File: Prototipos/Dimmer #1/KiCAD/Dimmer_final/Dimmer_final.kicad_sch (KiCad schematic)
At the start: 23 parts, among them J2 Conn_01x02, K1 SRD-05VDC-SL-C, Q1 BC548B, Q2 BT137, U1 MOC3021M, U2 EL817

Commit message: Retoques finales placa dimmer
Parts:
- added TP1, TP2: TestPoint, TestPoint:TestPoint_Loop_D1.80mm_Drill1.0mm_Beaded, symbol Connector:TestPoint
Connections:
- net 48Vca_L: now also TP1.1
- net LOAD_L: now also TP2.1
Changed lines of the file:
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@@
+	)
+	(junction
+		(at 59.69 82.55)
+		(diameter 0)
+		(color 0 0 0 0)
+	)
+	(junction
+		(at 53.34 40.64)
+		(diameter 0)
+		(color 0 0 0 0)
 	)
 	(junction
@@
 	(wire
 		(pts
+			(xy 59.69 82.55) (xy 63.5 82.55)
+		)
+		(stroke
+			(width 0)
+			(type default)
+		)
+	)
+	(wire
+		(pts
 			(xy 96.52 115.57) (xy 99.06 115.57)
 		)
@@
 	(wire
 		(pts
-			(xy 46.99 40.64) (xy 63.5 40.64)
+			(xy 46.99 40.64) (xy 53.34 40.64)
 		)
 		(stroke
@@
 	(wire
 		(pts
+			(xy 53.34 40.64) (xy 63.5 40.64)
+		)
+		(stroke
+			(width 0)
+			(type default)
+		)
+	)
+	(wire
+		(pts
 			(xy 107.95 115.57) (xy 104.14 115.57)
 		)
@@
 	(wire
 		(pts
-			(xy 57.15 82.55) (xy 63.5 82.55)
+			(xy 57.15 82.55) (xy 59.69 82.55)
 		)
 		(stroke
@@
 	)
 	(symbol
+		(lib_id "Connector:TestPoint")
+		(at 59.69 82.55 0)
+		(unit 1)
+		(exclude_from_sim no)
+		(in_bom yes)
+		(on_board yes)
+		(dnp no)
+		(property "Reference" "TP2"
+			(at 57.912 77.47 0)
+			(effects
+				(font
+					(size 1.27 1.27)
+				)
+				(justify left)
+			)
+		)
+		(property "Value" "TestPoint"
+			(at 53.34 79.502 0)
+			(effects
+				(font
+					(size 1.27 1.27)
+				)
+				(justify left)
+				(hide yes)
+			)
+		)
+		(property "Footprint" "TestPoint:TestPoint_Loop_D1.80mm_Drill1.0mm_Beaded"
+			(at 64.77 82.55 0)
+			(effects
+				(font
+					(size 1.27 1.27)
+				)
+				(hide yes)
+			)
+		)
+		(property "Datasheet" "~"
+			(at 64.77 82.55 0)
+			(effects
+				(font
+					(size 1.27 1.27)
+				)
+				(hide yes)
+			)
+		)
+		(property "Description" "test point"
+			(at 59.69 82.55 0)
+			(effects
+				(font
+					(size 1.27 1.27)
+				)
+				(hide yes)
+			)
+		)
+		(pin "1"
+		)
+		(instances
+			(project ""
+				(path "/7934e872-2b7f-4f8f-a0b6-741d97320597"
+					(reference "TP2")
+					(unit 1)
+				)
+			)
+		)
+	)
+	(symbol
 		(lib_id "Proyecto_Final:PCIE_x4_NSH")
 		(at 210.82 62.23 0)
@@
 					(unit 1)
 				)
+			)
+		)
+	)
+	(symbol
+		(lib_id "Connector:TestPoint")
+		(at 53.34 40.64 0)
+		(unit 1)
+		(exclude_from_sim no)
+		(in_bom yes)
+		(on_board yes)
+		(dnp no)
+		(property "Reference" "TP1"
+			(at 51.562 35.56 0)
+			(effects
+				(font
+					(size 1.27 1.27)
+				)
+				(justify left)
+			)
+		)
+		(property "Value" "TestPoint"
+			(at 55.88 38.6079 0)
+			(effects
+				(font
+					(size 1.27 1.27)
+				)
+				(justify left)
+				(hide yes)
+			)
+		)
+		(property "Footprint" "TestPoint:TestPoint_Loop_D1.80mm_Drill1.0mm_Beaded"
+			(at 58.42 40.64 0)
+			(effects
+				(font
+					(size 1.27 1.27)
+				)
+				(hide yes)
+			)
+		)
+		(property "Datasheet" "~"
+			(at 58.42 40.64 0)
+			(effects
+				(font
+					(size 1.27 1.27)
+				)
+				(hide yes)
+			)
+		)
+		(property "Description" "test point"
+			(at 53.34 40.64 0)
+			(effects
+				(font
+					(size 1.27 1.27)
+				)
+				(hide yes)
+			)
+		)
+		(pin "1"
+		)
+		(instances
+			(project ""
+				(path "/7934e872-2b7f-4f8f-a0b6-741d97320597"
+					(reference "TP1")
+					(unit 1)
+				)

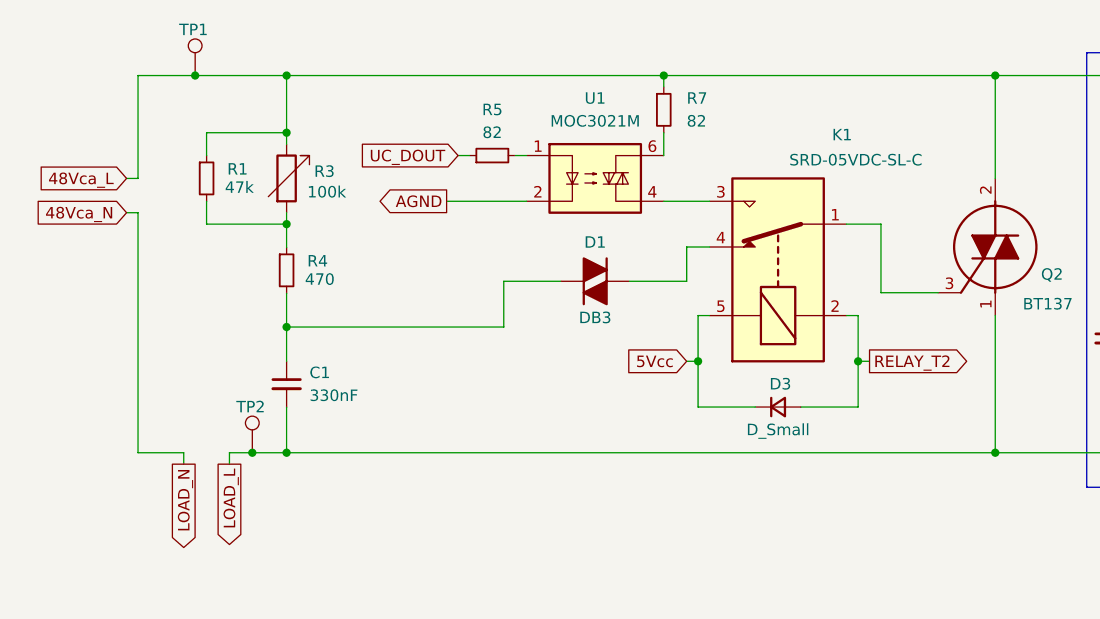
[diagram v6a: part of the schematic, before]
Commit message: Agregar TPs nuevos y correcciones varias
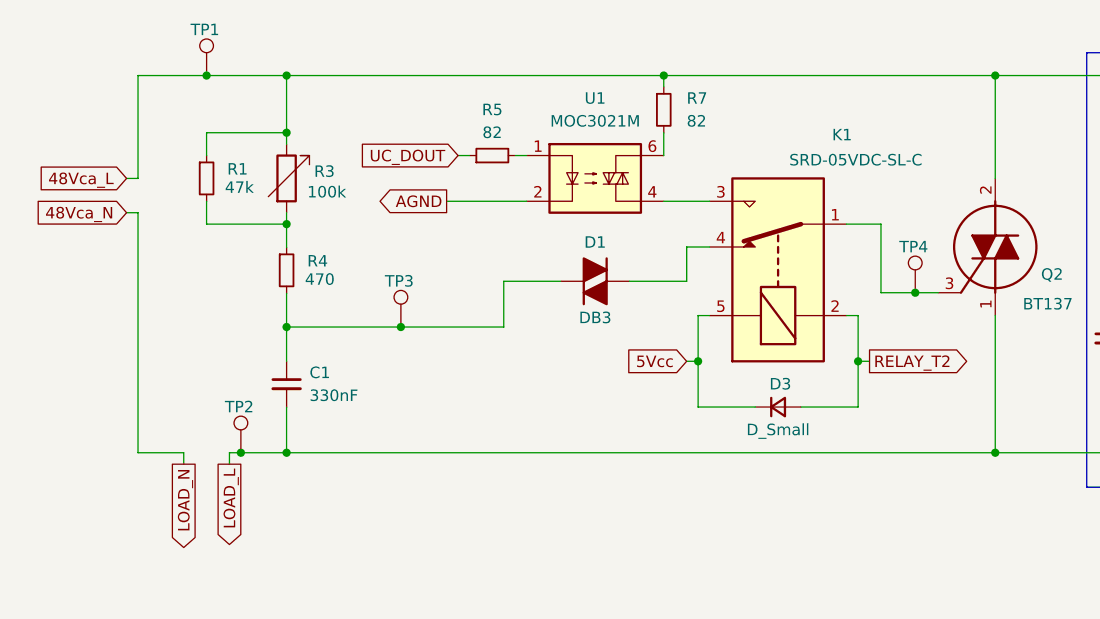
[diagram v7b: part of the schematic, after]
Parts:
- added TP3, TP4: TestPoint, TestPoint:TestPoint_Loop_D1.80mm_Drill1.0mm_Beaded, symbol Connector:TestPoint
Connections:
- net at C1.1, D1.1 (K), R4.2: now also TP3.1
- net at K1.1, Q2.3 (G): now also TP4.1
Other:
- moved on the sheet: TP1, TP2
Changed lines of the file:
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@@
 	)
 	(junction
-		(at 127 72.39)
+		(at 58.42 82.55)
 		(diameter 0)
 		(color 0 0 0 0)
 	)
 	(junction
-		(at 142.24 82.55)
+		(at 133.35 64.77)
 		(diameter 0)
 		(color 0 0 0 0)
 	)
 	(junction
-		(at 59.69 82.55)
+		(at 127 72.39)
 		(diameter 0)
 		(color 0 0 0 0)
 	)
 	(junction
-		(at 53.34 40.64)
+		(at 142.24 82.55)
 		(diameter 0)
 		(color 0 0 0 0)
@@
 	)
 	(junction
+		(at 76.2 68.58)
+		(diameter 0)
+		(color 0 0 0 0)
+	)
+	(junction
+		(at 54.61 40.64)
+		(diameter 0)
+		(color 0 0 0 0)
+	)
+	(junction
 		(at 63.5 68.58)
 		(diameter 0)
@@
 	(wire
 		(pts
-			(xy 105.41 54.61) (xy 110.49 54.61)
+			(xy 58.42 82.55) (xy 63.5 82.55)
 		)
 		(stroke
@@
 	(wire
 		(pts
-			(xy 154.94 72.39) (xy 154.94 82.55)
+			(xy 105.41 54.61) (xy 110.49 54.61)
 		)
 		(stroke
@@
 	(wire
 		(pts
-			(xy 120.65 77.47) (xy 127 77.47)
+			(xy 154.94 72.39) (xy 154.94 82.55)
 		)
 		(stroke
@@
 	(wire
 		(pts
-			(xy 59.69 82.55) (xy 63.5 82.55)
+			(xy 120.65 77.47) (xy 127 77.47)
 		)
 		(stroke
@@
 	(wire
 		(pts
-			(xy 46.99 40.64) (xy 53.34 40.64)
+			(xy 46.99 40.64) (xy 54.61 40.64)
+		)
+		(stroke
+			(width 0)
+			(type default)
+		)
+	)
+	(wire
+		(pts
+			(xy 133.35 64.77) (xy 135.89 64.77)
 		)
 		(stroke
@@
 	(wire
 		(pts
-			(xy 129.54 64.77) (xy 135.89 64.77)
+			(xy 129.54 64.77) (xy 133.35 64.77)
 		)
 		(stroke
@@
 	(wire
 		(pts
+			(xy 76.2 68.58) (xy 87.63 68.58)
+		)
+		(stroke
+			(width 0)
+			(type default)
+		)
+	)
+	(wire
+		(pts
 			(xy 129.54 124.46) (xy 132.08 124.46)
 		)
@@
 	(wire
 		(pts
-			(xy 63.5 68.58) (xy 87.63 68.58)
+			(xy 63.5 68.58) (xy 76.2 68.58)
 		)
 		(stroke
@@
 	(wire
 		(pts
-			(xy 53.34 40.64) (xy 63.5 40.64)
-		)
-		(stroke
-			(width 0)
-			(type default)
-		)
-	)
-	(wire
-		(pts
 			(xy 107.95 115.57) (xy 104.14 115.57)
 		)
@@
 	(wire
 		(pts
-			(xy 57.15 82.55) (xy 59.69 82.55)
+			(xy 57.15 82.55) (xy 58.42 82.55)
 		)
 		(stroke
@@
 	(wire
 		(pts
+			(xy 54.61 40.64) (xy 63.5 40.64)
+		)
+		(stroke
+			(width 0)
+			(type default)
+		)
+	)
+	(wire
+		(pts
 			(xy 87.63 63.5) (xy 93.98 63.5)
 		)
@@
 	(symbol
 		(lib_id "Connector:TestPoint")
-		(at 59.69 82.55 0)
+		(at 58.42 82.55 0)
 		(unit 1)
 		(exclude_from_sim no)
@@
 		(dnp no)
 		(property "Reference" "TP2"
-			(at 57.912 77.47 0)
+			(at 56.642 77.47 0)
 			(effects
 				(font
@@
 		)
 		(property "Value" "TestPoint"
-			(at 53.34 79.502 0)
+			(at 52.07 79.502 0)
 			(effects
 				(font
@@
 		)
 		(property "Footprint" "TestPoint:TestPoint_Loop_D1.80mm_Drill1.0mm_Beaded"
-			(at 64.77 82.55 0)
+			(at 63.5 82.55 0)
 			(effects
 				(font
@@
 		)
 		(property "Datasheet" "~"
-			(at 64.77 82.55 0)
+			(at 63.5 82.55 0)
 			(effects
 				(font
@@
 		)
 		(property "Description" "test point"
-			(at 59.69 82.55 0)
+			(at 58.42 82.55 0)
 			(effects
 				(font
@@
 	)
 	(symbol
+		(lib_id "Connector:TestPoint")
+		(at 133.35 64.77 0)
+		(unit 1)
+		(exclude_from_sim no)
+		(in_bom yes)
+		(on_board yes)
+		(dnp no)
+		(property "Reference" "TP4"
+			(at 131.572 59.69 0)
+			(effects
+				(font
+					(size 1.27 1.27)
+				)
+				(justify left)
+			)
+		)
+		(property "Value" "TestPoint"
+			(at 127 61.722 0)
+			(effects
+				(font
+					(size 1.27 1.27)
+				)
+				(justify left)
+				(hide yes)
+			)
+		)
+		(property "Footprint" "TestPoint:TestPoint_Loop_D1.80mm_Drill1.0mm_Beaded"
+			(at 138.43 64.77 0)
+			(effects
+				(font
+					(size 1.27 1.27)
+				)
+				(hide yes)
+			)
+		)
+		(property "Datasheet" "~"
+			(at 138.43 64.77 0)
+			(effects
+				(font
+					(size 1.27 1.27)
+				)
+				(hide yes)
+			)
+		)
+		(property "Description" "test point"
+			(at 133.35 64.77 0)
+			(effects
+				(font
+					(size 1.27 1.27)
+				)
+				(hide yes)
+			)
+		)
+		(pin "1"
+		)
+		(instances
+			(project "Dimmer_final"
+				(path "/7934e872-2b7f-4f8f-a0b6-741d97320597"
+					(reference "TP4")
+					(unit 1)
+				)
+			)
+		)
+	)
+	(symbol
 		(lib_id "Relay:SANYOU_SRD_Form_C")
 		(at 118.11 62.23 90)
@@
 	(symbol
 		(lib_id "Connector:TestPoint")
-		(at 53.34 40.64 0)
+		(at 76.2 68.58 0)
+		(unit 1)
+		(exclude_from_sim no)
+		(in_bom yes)
+		(on_board yes)
+		(dnp no)
+		(property "Reference" "TP3"
+			(at 74.422 63.5 0)
+			(effects
+				(font
+					(size 1.27 1.27)
+				)
+				(justify left)
+			)
+		)
+		(property "Value" "TestPoint"
+			(at 69.85 65.532 0)
+			(effects
+				(font
+					(size 1.27 1.27)
+				)
+				(justify left)
+				(hide yes)
+			)
+		)
+		(property "Footprint" "TestPoint:TestPoint_Loop_D1.80mm_Drill1.0mm_Beaded"
+			(at 81.28 68.58 0)
+			(effects
+				(font
+					(size 1.27 1.27)
+				)
+				(hide yes)
+			)
+		)
+		(property "Datasheet" "~"
+			(at 81.28 68.58 0)
+			(effects
+				(font
+					(size 1.27 1.27)
+				)
+				(hide yes)
+			)
+		)
+		(property "Description" "test point"
+			(at 76.2 68.58 0)
+			(effects
+				(font
+					(size 1.27 1.27)
+				)
+				(hide yes)
+			)
+		)
+		(pin "1"
+		)
+		(instances
+			(project "Dimmer_final"
+				(path "/7934e872-2b7f-4f8f-a0b6-741d97320597"
+					(reference "TP3")
+					(unit 1)
+				)
+			)
+		)
+	)
+	(symbol
+		(lib_id "Connector:TestPoint")
+		(at 54.61 40.64 0)
 		(unit 1)
 		(exclude_from_sim no)
@@
 		(dnp no)
 		(property "Reference" "TP1"
-			(at 51.562 35.56 0)
+			(at 52.832 35.56 0)
 			(effects
 				(font
@@
 		)
 		(property "Value" "TestPoint"
-			(at 55.88 38.6079 0)
+			(at 57.15 38.6079 0)
 			(effects
 				(font
@@
 		)
 		(property "Footprint" "TestPoint:TestPoint_Loop_D1.80mm_Drill1.0mm_Beaded"
-			(at 58.42 40.64 0)
+			(at 59.69 40.64 0)
 			(effects
 				(font
@@
 		)
 		(property "Datasheet" "~"
-			(at 58.42 40.64 0)
+			(at 59.69 40.64 0)
 			(effects
 				(font
@@
 		)
 		(property "Description" "test point"
-			(at 53.34 40.64 0)
+			(at 54.61 40.64 0)
 			(effects
 				(font

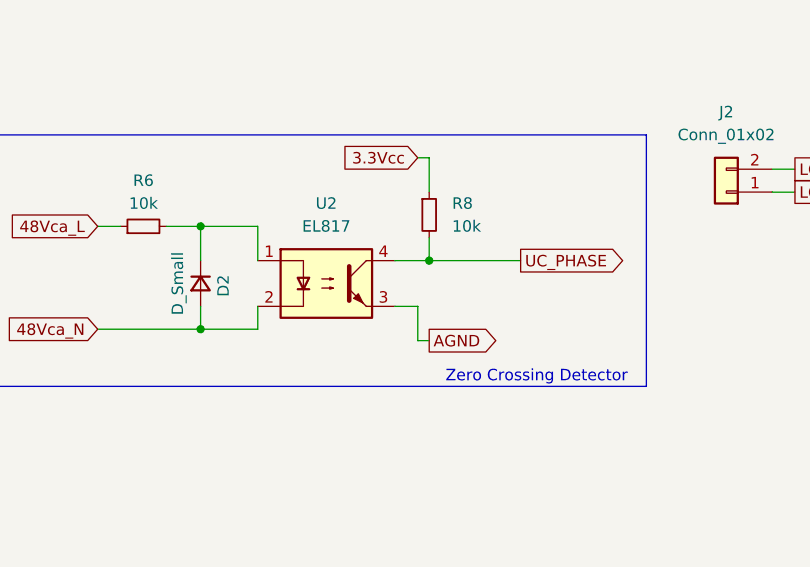
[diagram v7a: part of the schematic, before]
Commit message: Agregar nombre a diodos, cambiar UC por uC
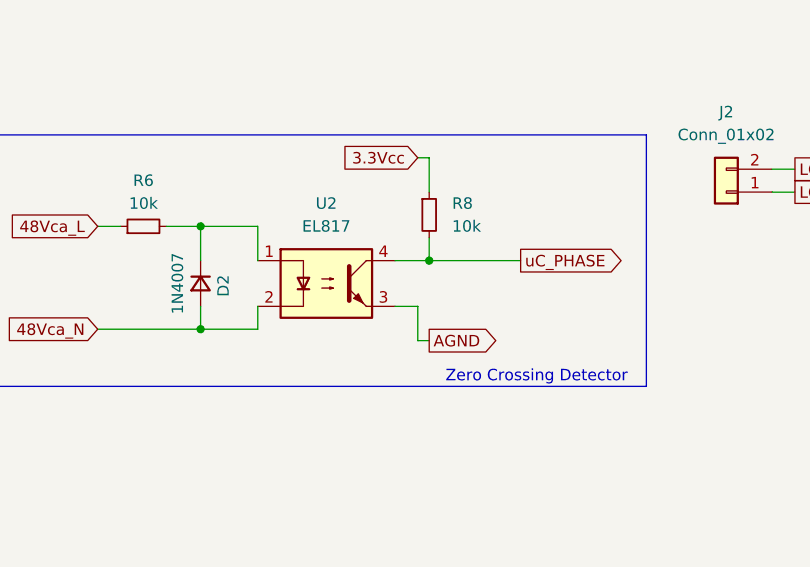
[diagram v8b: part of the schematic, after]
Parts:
- D2: value D_Small -> 1N4007
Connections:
- net UC_PHASE: no longer R8.2, U2.4
- new net uC_PHASE: R8.2, U2.4
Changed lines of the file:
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@@
 		)
 	)
-	(global_label "UC_PHASE"
+	(global_label "uC_PHASE"
 		(shape output)
 		(at 143.51 119.38 0)
@@
 		)
 		(property "Intersheetrefs" "${INTERSHEET_REFS}"
-			(at 156.1109 119.38 0)
+			(at 155.9294 119.38 0)
 			(effects
 				(font
@@
 			)
 		)
-		(property "Value" "D_Small"
+		(property "Value" "1N4007"
 			(at 105.41 121.92 0)
 			(effects
